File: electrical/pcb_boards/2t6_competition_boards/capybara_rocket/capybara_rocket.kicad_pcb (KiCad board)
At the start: 4 copper layers, 145 x 65 mm, 80 parts, among them J1 3.6V Battery, J10 Elevator, J11 SparkFun MAX-M10S, J12 Aileron 1, J13 Aileron 2, J14 Ground Camera, J15 Payload Camera, J16 DC Motor, J2 1.2V Battery, J3 3.6V Switch, J4 1.2V Switch, J5 LED, J6 NC, J7 CC, J8 VL53L1-SATEL, J9 Egg, U1 NE555P, U10 EEPROM, U11 STM32 NUCLEO-G431KB, U12 SparkFun XBee Explorer, U13 MAX756CPA+, U2 DS1307+, U3 Adafruit BNO085, U4 LTC3536, U5 MP3414, U6 Adafruit BMP581, U7 INA219, U8 DRV8212DRLR, U9 SN74LVC1G04DBVR, Y1 AB38T-32.768KHZ

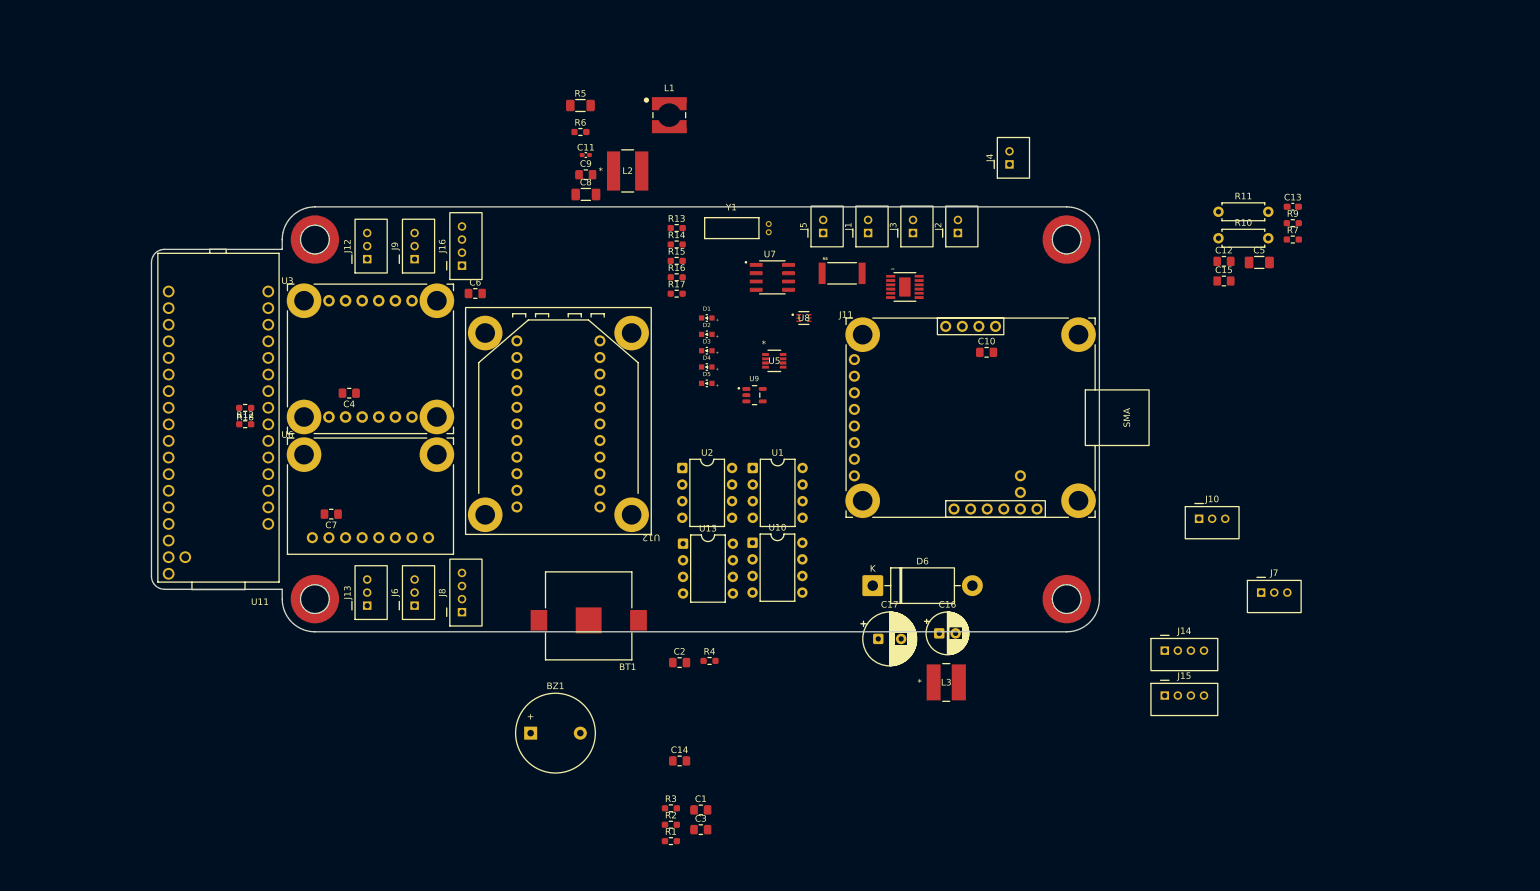
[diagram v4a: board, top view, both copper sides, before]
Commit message: Updates on component placements
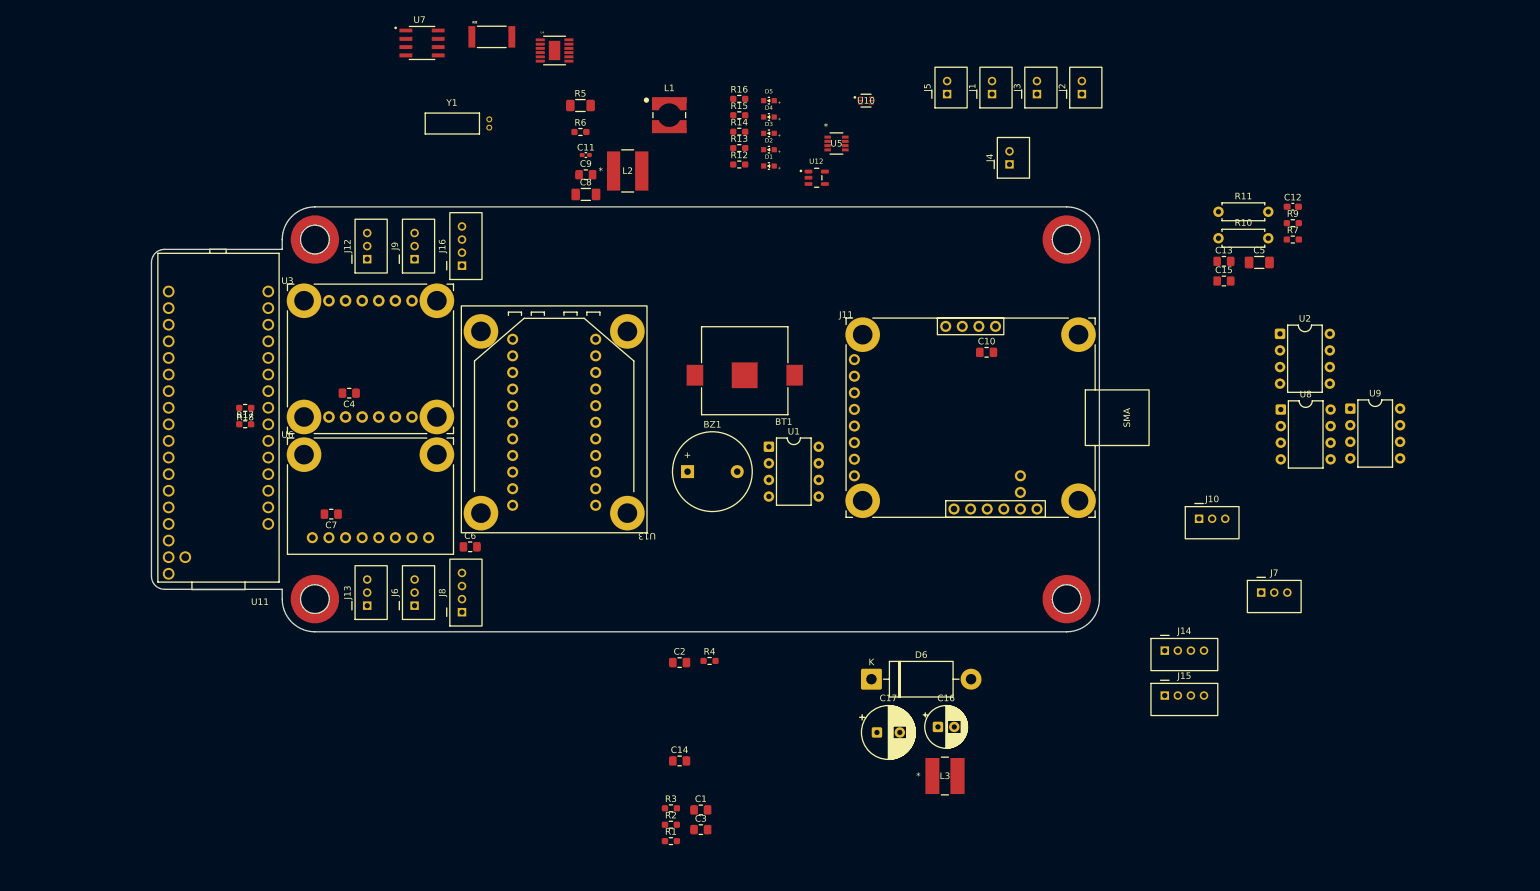
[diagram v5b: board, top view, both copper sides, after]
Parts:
- moved U2 93.7 mm to (250.1, 86.9)
- moved U8 93.7 mm to (250.2, 98.5)
- moved U9 93.7 mm to (260.9, 98.4)
- moved R8 64.7 mm to (129.6, 41.5)
- moved U4 64.7 mm to (139.2, 43.6)
- moved U7 64.5 mm to (118.9, 42.4)
- moved BZ1 46.6 mm to (159.5, 108.0)
- moved Y1 45.6 mm to (129.2, 54.8)
- moved BT1 44.5 mm to (168.2, 93.2)
- moved C6 38.8 mm to (126.2, 119.5)
- moved U10 34.6 mm to (186.8, 51.2)
- moved U5 34.6 mm to (182.3, 57.8)
- moved D1 34.6 mm to (171.9, 61.2)
- moved D2 34.6 mm to (171.9, 58.8)
- moved D3 34.6 mm to (171.9, 56.2)
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- renumbered C13 to C12, C12 to C13, D5 to D1, D4 to D2, D2 to D4, D1 to D5, R17 to R12, R16 to R13, R15 to R14, R14 to R15, R13 to R16, R12 to R17, U8 to U10, U9 to U12, U12 to U13, U13 to U8, U10 to U9

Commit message: PCB rearrangement update
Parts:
- REF** (x4): moved to B.Cu
- moved J14 144.0 mm to (100.0, 79.0)
- moved J15 128.3 mm to (106.0, 121.0), turned to 180 degrees
- moved J11 80.7 mm to (109.1, 115.2), turned to 180 degrees
- moved BT1 79.2 mm to (110.4, 147.2)
- moved U1 77.0 mm to (120.2, 161.2)
- moved R17 58.3 mm to (150.1, 100.8)
- moved R18 58.3 mm to (150.1, 98.3)
- moved U11 58.1 mm to (145.9, 99.8)
- moved U13 49.7 mm to (191.2, 85.2), turned to -90 degrees
- moved BZ1 46.0 mm to (129.0, 142.5)
- moved J12 37.7 mm to (73.2, 81.3)
- moved J9 37.5 mm to (80.8, 81.3)
- moved J16 37.3 mm to (87.8, 79.0), turned to 0 degrees
- moved J13 37.2 mm to (73.8, 122.8)
- moved J6 37.2 mm to (81.0, 122.8)
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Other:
- board size 145 x 65 mm -> 160 x 65 mm

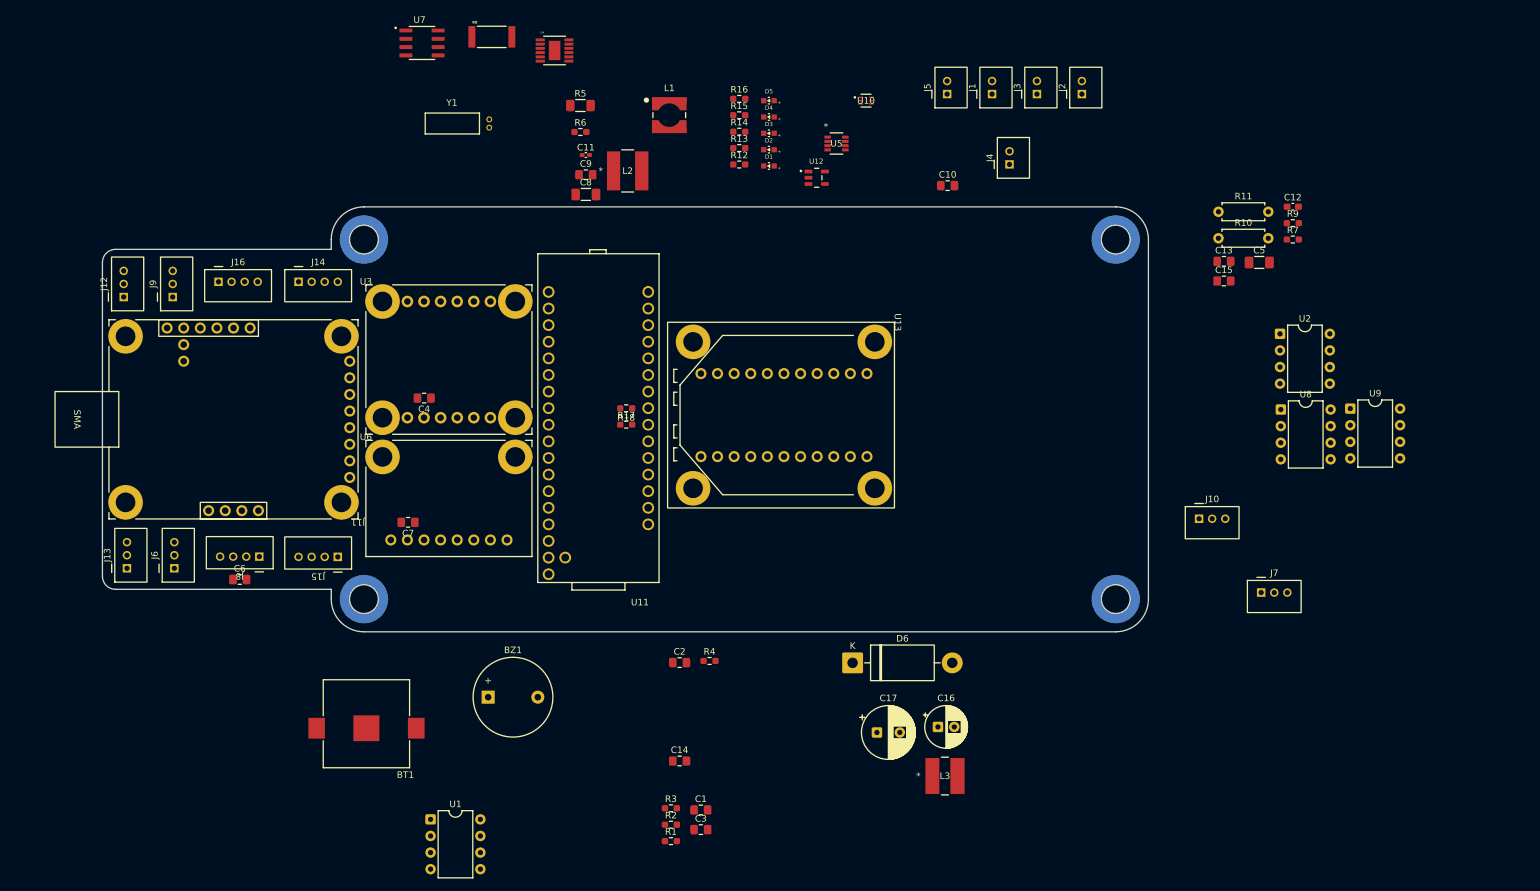
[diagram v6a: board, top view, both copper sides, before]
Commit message: Completed CPL schematic
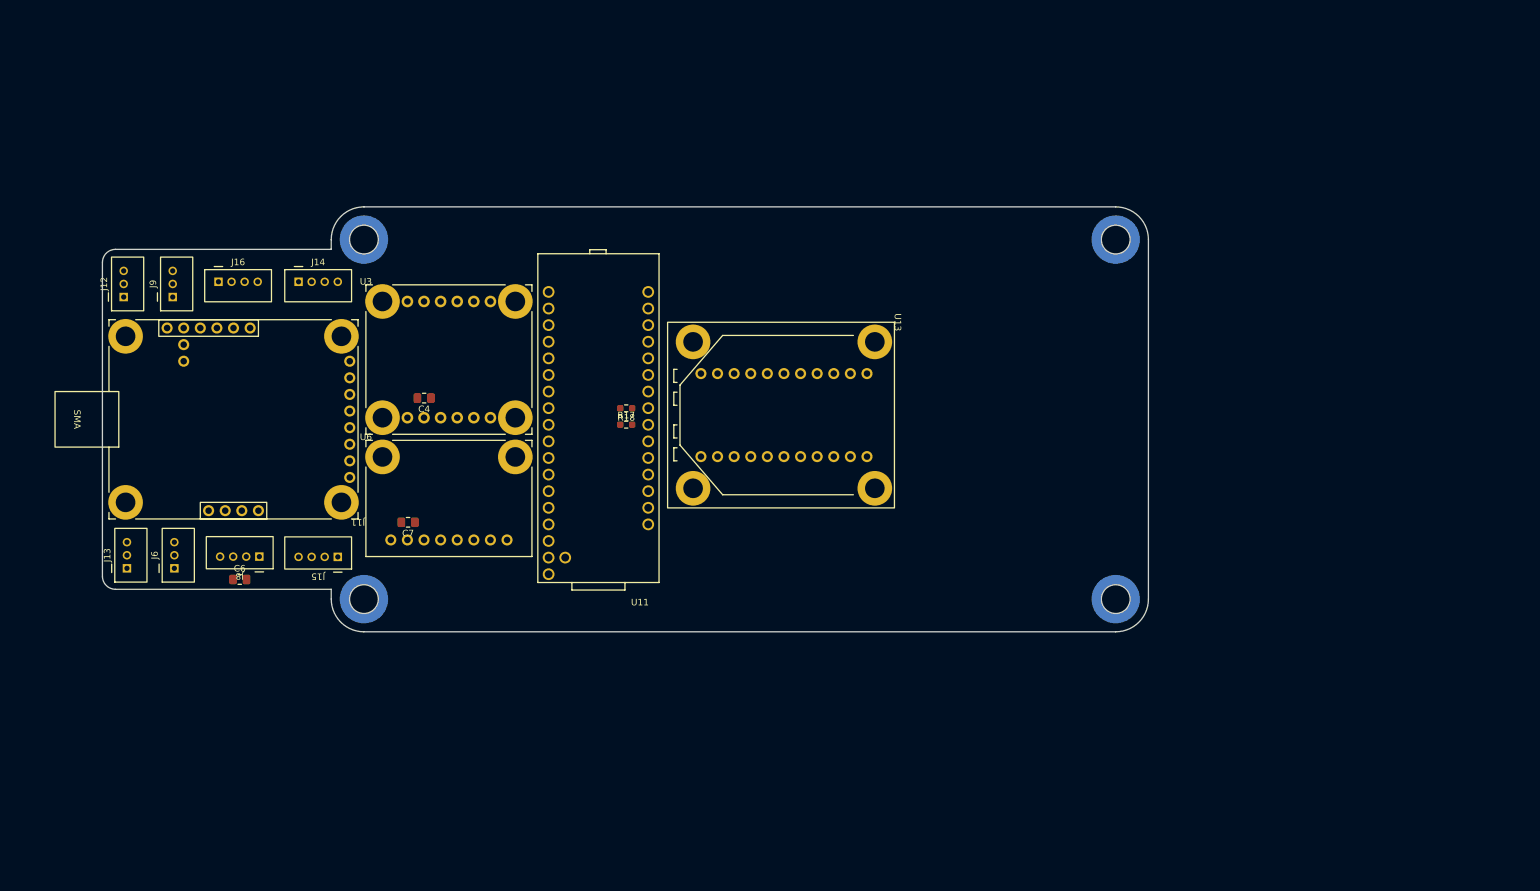
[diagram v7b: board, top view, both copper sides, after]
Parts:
- removed BT1: 2894TR, RSX_CanSat_Custom_KiCad_Footprints:BAT_2894TR
- removed BZ1: Buzzer, RSX_CanSat_Custom_KiCad_Footprints:Buzzer_12x9.5RM7.6
- removed C1, C3: 10μF, Capacitor_SMD:C_0805_2012Metric_Pad1.18x1.45mm_HandSolder
- removed C10, C14, C2: 0.1μF, Capacitor_SMD:C_0805_2012Metric_Pad1.18x1.45mm_HandSolder
- removed C11: 1μF, Capacitor_SMD:C_0402_1005Metric_Pad0.74x0.62mm_HandSolder
- removed C12: 47pF, Capacitor_SMD:C_0603_1608Metric_Pad1.08x0.95mm_HandSolder
- removed C13: 220pF, Capacitor_SMD:C_0805_2012Metric_Pad1.18x1.45mm_HandSolder
- removed C15, C9: 22μF, Capacitor_SMD:C_0805_2012Metric_Pad1.18x1.45mm_HandSolder
- removed C16: 150μF, Capacitor_THT:CP_Radial_D6.3mm_P2.50mm
- removed C17: 100μF, Capacitor_THT:CP_Radial_D8.0mm_P3.50mm
- removed C5, C8: 10μF, Capacitor_SMD:C_1206_3216Metric_Pad1.33x1.80mm_HandSolder
- removed D1, D2, D3, D4, D5: LED, DigiKey:WL-SMCW_0603
- removed D6: 1N5820, Diode_THT:D_DO-201AD_P15.24mm_Horizontal
- removed J1: 3.6V Battery, RSX_CanSat_Custom_KiCad_Footprints:J_Wurth_WR-WTB_62000211622
- removed J10: Elevator, RSX_CanSat_Custom_KiCad_Footprints:J_Wurth_WR-WTB_62000311622
- removed J2: 1.2V Battery, RSX_CanSat_Custom_KiCad_Footprints:J_Wurth_WR-WTB_62000211622
- removed J3: 3.6V Switch, RSX_CanSat_Custom_KiCad_Footprints:J_Wurth_WR-WTB_62000211622
- removed J4: 1.2V Switch, RSX_CanSat_Custom_KiCad_Footprints:J_Wurth_WR-WTB_62000211622
- removed J5: LED, RSX_CanSat_Custom_KiCad_Footprints:J_Wurth_WR-WTB_62000211622
- removed J7: CC, RSX_CanSat_Custom_KiCad_Footprints:J_Wurth_WR-WTB_62000311622
- removed L1: 15μH, RSX_CanSat_Custom_KiCad_Footprints:WE-TPC_4828
- removed L2: 2.2μH, RSX_CanSat_Custom_KiCad_Footprints:IND_BOURNS_SRN6045
- removed L3: 22μH, RSX_CanSat_Custom_KiCad_Footprints:IND_CD54_SUM
- removed R1: 1kΩ, Resistor_SMD:R_0603_1608Metric_Pad0.98x0.95mm_HandSolder
- removed R10: 221kΩ, Resistor_THT:R_Axial_DIN0207_L6.3mm_D2.5mm_P7.62mm_Horizontal
- removed R11: 1MΩ, Resistor_THT:R_Axial_DIN0207_L6.3mm_D2.5mm_P7.62mm_Horizontal
- removed R12, R13, R14, R15, R16: 100Ω, Resistor_SMD:R_0603_1608Metric_Pad0.98x0.95mm_HandSolder
- removed R2: 220Ω, Resistor_SMD:R_0603_1608Metric_Pad0.98x0.95mm_HandSolder
- removed R3, R4: 10Ω, Resistor_SMD:R_0603_1608Metric_Pad0.98x0.95mm_HandSolder
- removed R5: 61.9kΩ, Resistor_SMD:R_1206_3216Metric_Pad1.30x1.75mm_HandSolder
- removed R6: 505kΩ, Resistor_SMD:R_0603_1608Metric_Pad0.98x0.95mm_HandSolder
- removed R7: 51kΩ, Resistor_SMD:R_0603_1608Metric_Pad0.98x0.95mm_HandSolder
- removed R8: PT2512FK-070R1L, RSX_CanSat_Custom_KiCad_Footprints:RESC6331X65N
- removed R9: 6.2kΩ, Resistor_SMD:R_0603_1608Metric_Pad0.98x0.95mm_HandSolder
- removed U1: NE555P, Package_DIP:DIP-8_W7.62mm
- removed U10: DRV8212DRLR, RSX_CanSat_Custom_KiCad_Footprints:SOT6_DRV8212_TEX
- removed U12: SN74LVC1G04DBVR, RSX_CanSat_Custom_KiCad_Footprints:SOT95P280X145-5N
- removed U2: DS1307+, Package_DIP:DIP-8_W7.62mm
- removed U4: LTC3536, RSX_CanSat_Custom_KiCad_Footprints:MSOP-12_MSE
- removed U5: MP3414, RSX_CanSat_Custom_KiCad_Footprints:TSOT23-8_MP3414A
- removed U7: INA219, RSX_CanSat_Custom_KiCad_Footprints:SOIC127P599X175-8N
- removed U8: MAX756CPA+, Package_DIP:DIP-8_W7.62mm
- removed U9: EEPROM, Package_DIP:DIP-8_W7.62mm
- removed Y1: AB38T-32.768KHZ, RSX_CanSat_Custom_KiCad_Footprints:XTAL_AB38T-32.768KHZ

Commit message: Locking in sensor placements
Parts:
- added BT1: 2894TR, RSX_CanSat_Custom_KiCad_Footprints:BAT_2894TR, F.Cu at (264.3, 91.7)
- added BZ1: Buzzer, RSX_CanSat_Custom_KiCad_Footprints:Buzzer_12x9.5RM7.6, F.Cu at (277.0, 91.6)
- added C1: 20μF, Capacitor_SMD:C_0805_2012Metric_Pad1.18x1.45mm_HandSolder, F.Cu at (276.1, 101.3)
- added C10: 47pF, Capacitor_SMD:C_0603_1608Metric_Pad1.08x0.95mm_HandSolder, F.Cu at (262.9, 101.1)
- added C11: 220pF, Capacitor_SMD:C_0805_2012Metric_Pad1.18x1.45mm_HandSolder, F.Cu at (276.1, 113.4)
- added C12: 47pF, Capacitor_SMD:C_0603_1608Metric_Pad1.08x0.95mm_HandSolder, F.Cu at (262.9, 103.6)
- added C13: 220pF, Capacitor_SMD:C_0805_2012Metric_Pad1.18x1.45mm_HandSolder, F.Cu at (280.9, 101.3)
- added C14: 0.1μF, Capacitor_SMD:C_0805_2012Metric_Pad1.18x1.45mm_HandSolder, F.Cu at (280.9, 104.4)
- added C15: 22μF, Capacitor_SMD:C_0805_2012Metric_Pad1.18x1.45mm_HandSolder, F.Cu at (280.9, 107.4)
- added C16: 22μF, Capacitor_SMD:C_0805_2012Metric_Pad1.18x1.45mm_HandSolder, F.Cu at (280.9, 110.4)
- added C17: 10μF, Capacitor_SMD:C_1206_3216Metric_Pad1.33x1.80mm_HandSolder, F.Cu at (257.7, 108.2)
- added C18: 22μF, Capacitor_SMD:C_0805_2012Metric_Pad1.18x1.45mm_HandSolder, F.Cu at (280.9, 113.4)
- added C19: 10μF, Capacitor_SMD:C_1206_3216Metric_Pad1.33x1.80mm_HandSolder, F.Cu at (257.7, 111.6)
- added C2: 0.1μF, Capacitor_SMD:C_0805_2012Metric_Pad1.18x1.45mm_HandSolder, F.Cu at (276.1, 104.4)
- added C20: 1μF, Capacitor_SMD:C_0402_1005Metric_Pad0.74x0.62mm_HandSolder, F.Cu at (241.8, 125.5)
- added C21: 10μF, Capacitor_SMD:C_1206_3216Metric_Pad1.33x1.80mm_HandSolder, F.Cu at (257.7, 114.9)
- added C4: 10μF, Capacitor_SMD:C_0805_2012Metric_Pad1.18x1.45mm_HandSolder, F.Cu at (276.1, 107.4)
- added C5: 10μF, Capacitor_SMD:C_1206_3216Metric_Pad1.33x1.80mm_HandSolder, F.Cu at (257.7, 101.5)
- added C6: 10μF, Capacitor_SMD:C_1206_3216Metric_Pad1.33x1.80mm_HandSolder, F.Cu at (257.7, 104.9)
- added C9: 0.1μF, Capacitor_SMD:C_0805_2012Metric_Pad1.18x1.45mm_HandSolder, F.Cu at (276.1, 110.4)
- added D1: LED, DigiKey:WL-SMCW_0603, F.Cu at (285.3, 101.1)
- added D2: LED, DigiKey:WL-SMCW_0603, F.Cu at (285.3, 103.6)
- added D3: LED, DigiKey:WL-SMCW_0603, F.Cu at (285.3, 106.1)
- added D4: LED, DigiKey:WL-SMCW_0603, F.Cu at (285.3, 108.6)
- added D5: LED, DigiKey:WL-SMCW_0603, F.Cu at (285.3, 111.1)
- added D6: LED, DigiKey:WL-SMCW_0603, F.Cu at (285.3, 113.6)
- added J1: 3.6V Battery, RSX_CanSat_Custom_KiCad_Footprints:J_Wurth_WR-WTB_62000211622, F.Cu at (238.9, 76.0)
- added J10: Elevator, RSX_CanSat_Custom_KiCad_Footprints:J_Wurth_WR-WTB_62000311622, F.Cu at (263.7, 124.7)
- added J2: 1.2V Battery, RSX_CanSat_Custom_KiCad_Footprints:J_Wurth_WR-WTB_62000211622, F.Cu at (238.9, 82.9)
- added J3: 3.6V Switch, RSX_CanSat_Custom_KiCad_Footprints:J_Wurth_WR-WTB_62000211622, F.Cu at (238.9, 89.8)
- added J4: 1.2V Switch, RSX_CanSat_Custom_KiCad_Footprints:J_Wurth_WR-WTB_62000211622, F.Cu at (238.9, 96.6)
- added J5: LED, RSX_CanSat_Custom_KiCad_Footprints:J_Wurth_WR-WTB_62000211622, F.Cu at (238.9, 103.5)
- added J7: CC, RSX_CanSat_Custom_KiCad_Footprints:J_Wurth_WR-WTB_62000311622, F.Cu at (263.7, 117.8)
- added L1: 15μH, RSX_CanSat_Custom_KiCad_Footprints:WE-TPC_4828, F.Cu at (278.1, 118.4)
- added L2: 15μH, RSX_CanSat_Custom_KiCad_Footprints:WE-TPC_4828, F.Cu at (278.1, 125.4)
- added L3: 2.2μH, RSX_CanSat_Custom_KiCad_Footprints:IND_BOURNS_SRN6045, F.Cu at (239.8, 111.4)
- added L4: 4.7μH, RSX_CanSat_Custom_KiCad_Footprints:IND_B82462G4472M000, F.Cu at (248.2, 113.8)
- added Q1: SI4435DDY, Package_SO:SOIC-8_3.9x4.9mm_P1.27mm, F.Cu at (248.1, 121.1)
- added R1: 100kΩ, Resistor_SMD:R_0603_1608Metric_Pad0.98x0.95mm_HandSolder, F.Cu at (262.9, 106.1)
- added R10: 221kΩ, Resistor_THT:R_Axial_DIN0207_L6.3mm_D2.5mm_P7.62mm_Horizontal, F.Cu at (245.5, 90.9)
- added R11: 1MΩ, Resistor_THT:R_Axial_DIN0207_L6.3mm_D2.5mm_P7.62mm_Horizontal, F.Cu at (245.5, 95.0)
- added R12: 1MΩ, Resistor_THT:R_Axial_DIN0207_L6.3mm_D2.5mm_P7.62mm_Horizontal, F.Cu at (245.5, 99.0)
- added R13: 61.9kΩ, Resistor_SMD:R_1206_3216Metric_Pad1.30x1.75mm_HandSolder, F.Cu at (238.8, 117.0)
- added R14: 100Ω, Resistor_SMD:R_0603_1608Metric_Pad0.98x0.95mm_HandSolder, F.Cu at (267.2, 108.6)
- added R15: 100Ω, Resistor_SMD:R_0603_1608Metric_Pad0.98x0.95mm_HandSolder, F.Cu at (267.2, 111.1)
- added R16: 100Ω, Resistor_SMD:R_0603_1608Metric_Pad0.98x0.95mm_HandSolder, F.Cu at (267.2, 113.6)
- added R17: 100Ω, Resistor_SMD:R_0603_1608Metric_Pad0.98x0.95mm_HandSolder, F.Cu at (271.6, 101.1)
- added R18: 100Ω, Resistor_SMD:R_0603_1608Metric_Pad0.98x0.95mm_HandSolder, F.Cu at (271.6, 103.6)
- added R19: 100Ω, Resistor_SMD:R_0603_1608Metric_Pad0.98x0.95mm_HandSolder, F.Cu at (271.6, 106.1)
- added R2: 5.1kΩ, Resistor_SMD:R_0603_1608Metric_Pad0.98x0.95mm_HandSolder, F.Cu at (262.9, 108.6)
- added R20: 505kΩ, Resistor_SMD:R_0603_1608Metric_Pad0.98x0.95mm_HandSolder, F.Cu at (271.6, 108.6)
- added R23: 100kΩ, Resistor_THT:R_Axial_DIN0207_L6.3mm_D2.5mm_P7.62mm_Horizontal, F.Cu at (245.5, 103.1)
- added R24: 976kΩ, Resistor_SMD:R_0805_2012Metric_Pad1.20x1.40mm_HandSolder, F.Cu at (238.2, 120.1)
- added R25: 562kΩ, Resistor_SMD:R_0805_2012Metric_Pad1.20x1.40mm_HandSolder, F.Cu at (238.2, 123.1)
- added R3: 10Ω, Resistor_SMD:R_0603_1608Metric_Pad0.98x0.95mm_HandSolder, F.Cu at (262.9, 111.1)
- added R4: 51kΩ, Resistor_SMD:R_0603_1608Metric_Pad0.98x0.95mm_HandSolder, F.Cu at (262.9, 113.6)
- added R5: 51kΩ, Resistor_SMD:R_0603_1608Metric_Pad0.98x0.95mm_HandSolder, F.Cu at (267.2, 101.1)
- added R6: PT2512FK-070R1L, RSX_CanSat_Custom_KiCad_Footprints:RESC6331X65N, F.Cu at (248.3, 107.5)
- added R7: 6.2kΩ, Resistor_SMD:R_0603_1608Metric_Pad0.98x0.95mm_HandSolder, F.Cu at (267.2, 103.6)
- added R8: 6.2kΩ, Resistor_SMD:R_0603_1608Metric_Pad0.98x0.95mm_HandSolder, F.Cu at (267.2, 106.1)
- added R9: 221kΩ, Resistor_THT:R_Axial_DIN0207_L6.3mm_D2.5mm_P7.62mm_Horizontal, F.Cu at (245.5, 86.9)
- added U1: DS1307+, Package_DIP:DIP-8_W7.62mm, F.Cu at (245.5, 75.2)
- added U10: MP3414, RSX_CanSat_Custom_KiCad_Footprints:TSOT23-8_MP3414A, F.Cu at (257.4, 123.7)
- added U11: SN74LVC1G04, RSX_CanSat_Custom_KiCad_Footprints:SOT95P280X145-5N, F.Cu at (247.0, 126.5)
- added U12: MCP1640, RSX_CanSat_Custom_KiCad_Footprints:SOT-23-6_MC_MCH, F.Cu at (257.5, 119.0)
- added U13: EEPROM, Package_DIP:DIP-8_W7.62mm, F.Cu at (267.0, 75.2)
- added U3: TLC555, Package_DIP:DIP-8_W7.62mm, F.Cu at (256.3, 75.2)
- added U4: LTC3536, RSX_CanSat_Custom_KiCad_Footprints:MSOP-12_MSE, F.Cu at (285.0, 117.7)
- added U5: LTC3536, RSX_CanSat_Custom_KiCad_Footprints:MSOP-12_MSE, F.Cu at (285.0, 123.2)
- added U7: DRV8212DRLR, RSX_CanSat_Custom_KiCad_Footprints:SOT6_DRV8212_TEX, F.Cu at (91.4, 83.0)
- added U8: INA219, RSX_CanSat_Custom_KiCad_Footprints:SOIC127P599X175-8N, F.Cu at (281.0, 81.1)
- added U9: TPS3839, Package_TO_SOT_SMD:SOT-23, F.Cu at (252.1, 126.5)
- added Y1: AB38T-32.768KHZ, RSX_CanSat_Custom_KiCad_Footprints:XTAL_AB38T-32.768KHZ, F.Cu at (286.8, 75.5)
- moved C7 7.31 mm to (91.4, 117.2)
- moved J16 1.00 mm to (88.4, 78.2)
- moved J8 0.89 mm to (94.4, 121.8)
- moved J14 0.88 mm to (100.5, 78.2)
- moved J15 0.88 mm to (106.5, 121.8)
- moved J12 0.76 mm to (74.0, 81.4)
- moved U15 0.67 mm to (191.0, 85.8)
- moved J9 0.66 mm to (81.4, 81.4)
- moved J6 0.44 mm to (81.4, 122.6)
- moved U2 0.43 mm to (110.2, 79.0)
- moved J13 0.31 mm to (74.0, 122.6)
- moved C8 0.26 mm to (116.6, 116.0)
- moved U14 0.23 mm to (146.0, 100.0)
- moved R21 0.20 mm to (150.1, 101.0)
- moved R22 0.16 mm to (150.1, 98.5)
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- renumbered C4 to C3, C6 to C7, C7 to C8, R17 to R21, R18 to R22, U11 to U14, U13 to U15, U3 to U2
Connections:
- J16 pad 2: WING_PWM -> DC_PWM_1
- J16 pad 3: WING_DIR -> DC_PWM_2
- U14 pad CN3_1: 3.3V -> 3.3V MCU
- U14 pad CN3_11: WING_PWM -> INV_PWM_1
- U14 pad CN3_12: WING_DIR -> INV_PWM_2
